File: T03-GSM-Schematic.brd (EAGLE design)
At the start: 33.9 x 80.5 mm, 19 parts, among them IC1 788TV, J1 POWER_JACKPTH_BREAD, J2 AVR, Q2 16M, U1 ATMEGA328P-PU

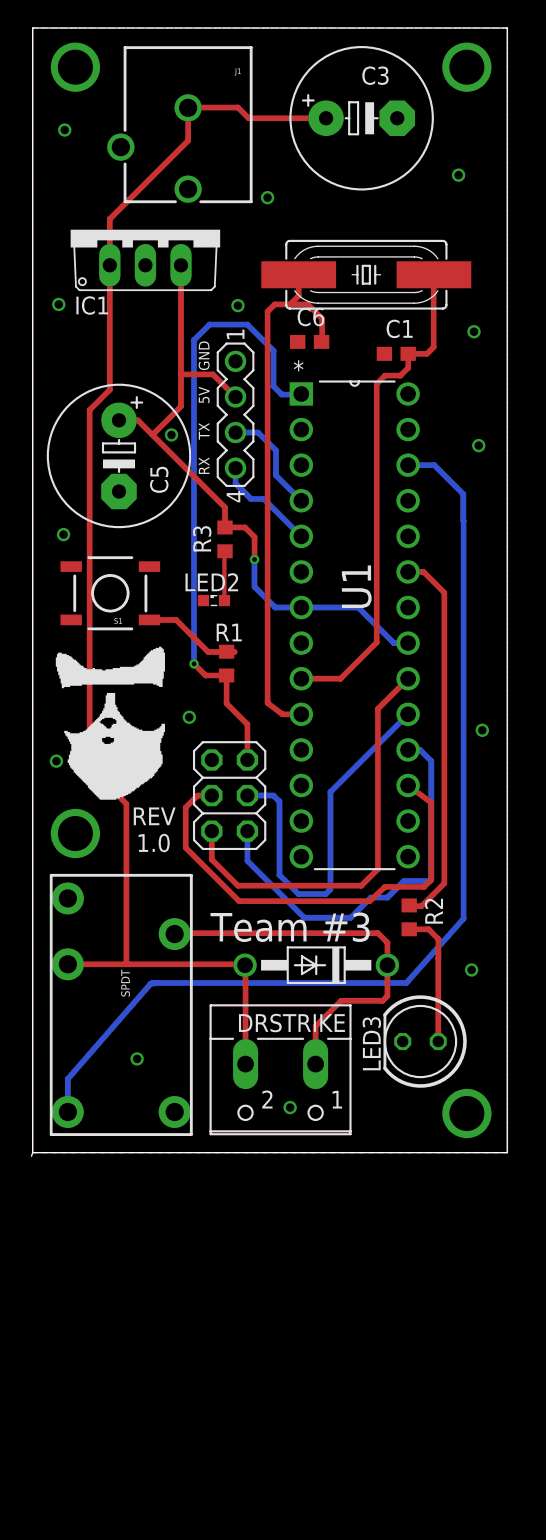
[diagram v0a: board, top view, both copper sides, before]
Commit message: Add files via upload
added flyback diode, bypass caps.  No board level work done yet.
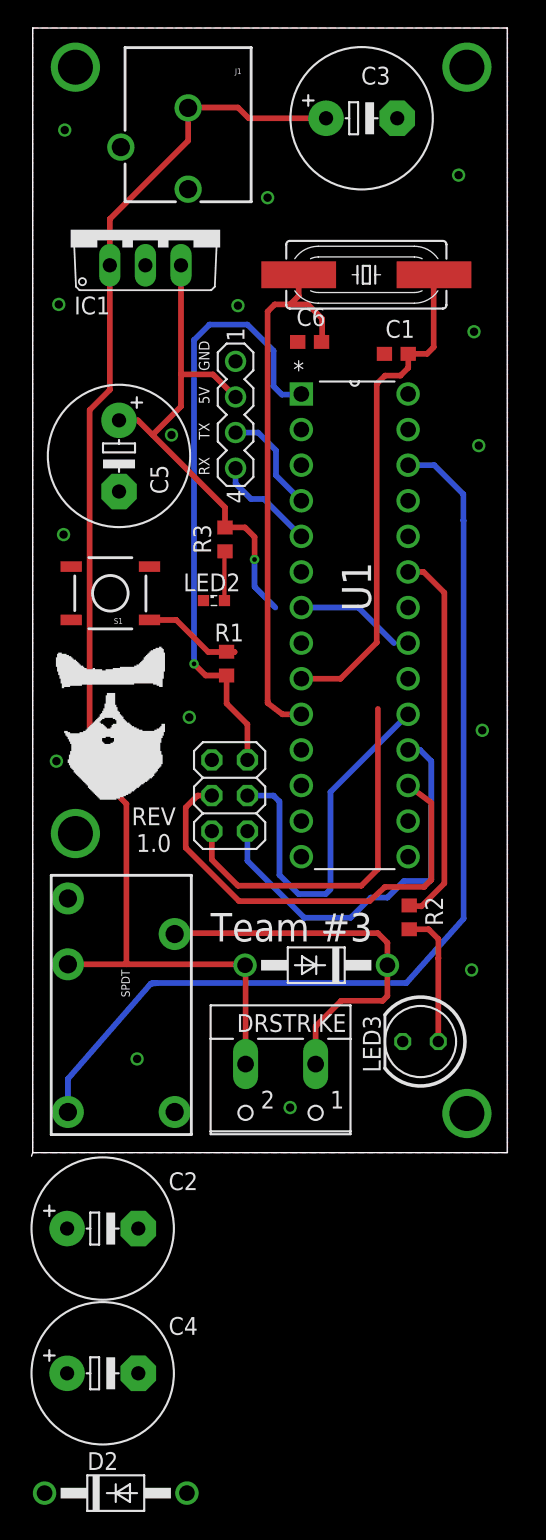
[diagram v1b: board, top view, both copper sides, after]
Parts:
- added C2, C4: 100n, rcl:E5-10,5
- added D2: 1N4004, diode:DO41-10
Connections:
- net 12V renamed +12V
- removed net 5V: C5.+, IC1.3, J2.2, R3.2, SV1.2, U1.20, U1.21, U1.7
- new net +5V: C2.+, C4.+, C5.+, IC1.3, J2.2, R3.2, SV1.2
- new net N$1: C2.-, U1.20, U1.21
- new net N$11: C4.-, U1.7
- net GND: now also D2.A
- net N$14: now also D2.C
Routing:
- net 5V: track 77.3 -> 0.00 mm, vias 1 -> 0
- net +5V: track 0.00 -> 63.7 mm, vias 0 -> 1
- net N$11: track 0.00 -> 7.66 mm

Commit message: Changed the layout of the PCB board
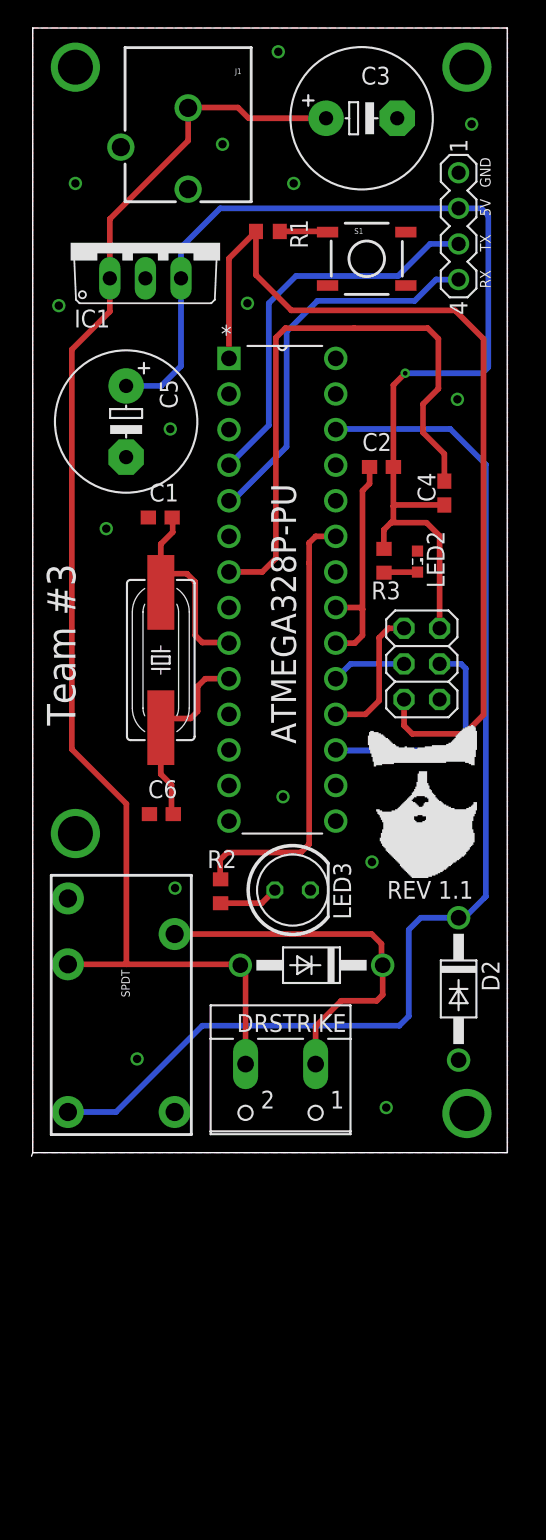
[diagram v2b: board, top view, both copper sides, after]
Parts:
- C2, C4: device rcl:E5-10,5 -> rcl:C0603
- moved C4 67.4 mm to (29.4, 47.1), turned to 90 degrees
- moved C2 57.9 mm to (24.9, 48.9), turned to 180 degrees
- moved D2 43.5 mm to (30.4, 11.7), turned to 270 degrees
- moved C6 35.3 mm to (9.18, 24.2)
- moved Q2 31.2 mm to (9.14, 35.2), turned to 90 degrees
- moved R1 31.0 mm to (16.8, 65.7), turned to 180 degrees
- moved S1 30.1 mm to (23.8, 63.8), turned to 0 degrees
- moved SV1 20.8 mm to (30.4, 66.1)
- moved C1 20.5 mm to (9.10, 45.3)
- moved J2 16.6 mm to (27.8, 34.9), turned to 270 degrees
- moved LED2 14.8 mm to (27.5, 42.2), turned to 270 degrees
- moved LED3 14.1 mm to (18.5, 18.7), turned to 0 degrees
- moved R2 13.6 mm to (13.4, 18.7)
- moved R3 11.4 mm to (25.1, 42.2)
- moved U1 5.75 mm to (21.6, 23.7)
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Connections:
- net +5V: now also C2.1, C4.1; no longer C2.+, C4.+
- net N$1: now also C2.2; no longer C2.-
- net N$11: now also C4.2; no longer C4.-
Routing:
- net N$11: track 7.66 -> 42.9 mm
- net N$18: track 39.6 -> 13.9 mm
- net N$10: track 44.1 -> 66.3 mm, vias 1 -> 0
- net N$5: track 26.8 -> 5.31 mm
- net N$16: track 35.8 -> 14.9 mm
- net RX: track 7.35 -> 27.7 mm
- net TX: track 7.75 -> 28.0 mm
- net N$8: track 28.5 -> 10.0 mm
- net +5V: track 63.7 -> 80.5 mm
- net N$1: track 0.00 -> 16.3 mm
- net N$7: track 32.4 -> 16.6 mm
- net N$14: track 71.3 -> 82.4 mm
- net N$6: track 9.69 -> 4.26 mm
- net N$9: track 27.1 -> 31.8 mm
- net N$2: track 7.59 -> 3.43 mm
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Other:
- board text added: "REV 1.1"
- board text removed: "REV 1.0"

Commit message: Add files via upload
Added test point, fixed ERC error.
More updates to come.
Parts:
- added R4: 0, rcl:0204/5
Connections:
- new net N$12: R4.2, U1.28
- net GND: now also R4.1
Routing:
- net N$6: track 4.26 -> 0.00 mm
- net N$12: track 0.00 -> 4.13 mm
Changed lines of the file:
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@@
 <?xml version="1.0" encoding="utf-8"?>
 <!DOCTYPE eagle SYSTEM "eagle.dtd">
-<eagle version="7.7.0">
+<eagle version="7.6.0">
 <drawing>
 <settings>
@@
 <element name="C4" library="rcl" package="C0603" value="100n" x="29.376390625" y="47.06995625" rot="R90"/>
 <element name="D2" library="diode" package="DO41-10" value="1N4004" x="30.392290625" y="11.68285" rot="R270"/>
+<element name="R4" library="rcl" package="0204/5" value="0" x="28.106521875" y="57.144284375" smashed="yes" rot="R180">
+<attribute name="NAME" x="28.673934375" y="57.584390625" size="0.9906" layer="25" ratio="10" rot="R180"/>
+<attribute name="VALUE" x="29.732175" y="57.59320625" size="0.9906" layer="27" ratio="10" rot="R180"/>
+</element>
 </elements>
 <signals>
@@
 <via x="10.158984375" y="18.878778125" extent="1-16" drill="0.6"/>
 <contactref element="D2" pad="A"/>
+<contactref element="R4" pad="1"/>
+<wire x1="30.392290625" y1="69.92805" x2="31.32353125" y2="73.398665625" width="0" layer="19" extent="1-1"/>
+<wire x1="26.013709375" y1="73.816803125" x2="31.32353125" y2="73.398665625" width="0" layer="19" extent="1-1"/>
+<wire x1="18.624803125" y1="69.16575" x2="26.013709375" y2="73.816803125" width="0" layer="19" extent="1-1"/>
+<wire x1="13.5453125" y1="71.959471875" x2="18.624803125" y2="69.16575" width="0" layer="19" extent="1-1"/>
+<wire x1="11.090225" y1="68.75708125" x2="13.5453125" y2="71.959471875" width="0" layer="19" extent="1-1"/>
+<wire x1="8.042528125" y1="62.3928375" x2="11.090225" y2="68.75708125" width="0" layer="19" extent="1-1"/>
+<wire x1="1.862484375" y1="60.445959375" x2="8.042528125" y2="62.3928375" width="0" layer="19" extent="1-1"/>
+<wire x1="15.3231375" y1="60.615278125" x2="8.042528125" y2="62.3928375" width="0" layer="19" extent="1-1"/>
+<wire x1="21.04239375" y1="61.88321875" x2="15.3231375" y2="60.615278125" width="0" layer="19" extent="1-1"/>
+<wire x1="17.52424375" y1="78.56281875" x2="13.5453125" y2="71.959471875" width="0" layer="19" extent="1-1"/>
+<wire x1="3.047696875" y1="69.165753125" x2="11.090225" y2="68.75708125" width="0" layer="19" extent="1-1"/>
+<wire x1="9.82035" y1="51.641496875" x2="15.3231375" y2="60.615278125" width="0" layer="19" extent="1-1"/>
+<wire x1="6.667271875" y1="49.634525" x2="9.82035" y2="51.641496875" width="0" layer="19" extent="1-1"/>
+<wire x1="8.250834375" y1="45.323878125" x2="6.667271875" y2="49.634525" width="0" layer="19" extent="1-1"/>
+<wire x1="5.2488125" y1="44.530215625" x2="8.250834375" y2="45.323878125" width="0" layer="19" extent="1-1"/>
+<wire x1="14.00585" y1="38.899746875" x2="8.250834375" y2="45.323878125" width="0" layer="19" extent="1-1"/>
+<wire x1="21.62585" y1="41.439746875" x2="14.00585" y2="38.899746875" width="0" layer="19" extent="1-1"/>
+<wire x1="27.460459375" y1="42.92720625" x2="21.62585" y2="41.439746875" width="0" layer="19" extent="1-1"/>
+<wire x1="29.03788125" y1="32.339171875" x2="27.460459375" y2="42.92720625" width="0" layer="19" extent="1-1"/>
+<wire x1="30.30763125" y1="53.75795625" x2="27.460459375" y2="42.92720625" width="0" layer="19" extent="1-1"/>
+<wire x1="24.2122375" y1="20.741265625" x2="29.03788125" y2="32.339171875" width="0" layer="19" extent="1-1"/>
+<wire x1="19.81871875" y1="18.738953125" x2="24.2122375" y2="20.741265625" width="0" layer="19" extent="1-1"/>
+<wire x1="17.862878125" y1="25.397453125" x2="19.81871875" y2="18.738953125" width="0" layer="19" extent="1-1"/>
+<wire x1="8.331021875" y1="24.159325" x2="17.862878125" y2="25.397453125" width="0" layer="19" extent="1-1"/>
+<wire x1="10.158984375" y1="18.878778125" x2="8.331021875" y2="24.159325" width="0" layer="19" extent="1-1"/>
+<wire x1="2.51" y1="18.14" x2="10.158984375" y2="18.878778125" width="0" layer="19" extent="1-1"/>
+<wire x1="7.44991875" y1="6.688" x2="10.158984375" y2="18.878778125" width="0" layer="19" extent="1-1"/>
+<wire x1="10.13" y1="2.9" x2="7.44991875" y2="6.688" width="0" layer="19" extent="1-1"/>
+<wire x1="30.646521875" y1="57.144284375" x2="10.13" y2="2.9" width="0" layer="19" extent="1-1"/>
+<wire x1="25.22814375" y1="3.217021875" x2="10.13" y2="2.9" width="0" layer="19" extent="1-1"/>
+<wire x1="30.392290625" y1="6.60285" x2="25.22814375" y2="3.217021875" width="0" layer="19" extent="1-1"/>
 </signal>
 <signal name="N$3">
@@
 <wire x1="24.889509375" y1="13.461165625" x2="24.974678125" y2="13.375996875" width="0.4064" layer="1"/>
 </signal>
-<signal name="N$6">
-<contactref element="R2" pad="2"/>
-<contactref element="LED3" pad="A"/>
-<wire x1="13.4077375" y1="17.8025625" x2="16.342328125" y2="17.8025625" width="0.4064" layer="1"/>
-<wire x1="16.342328125" y1="17.8025625" x2="17.27871875" y2="18.738953125" width="0.4064" layer="1"/>
-</signal>
 <signal name="N$9">
 <contactref element="R2" pad="1"/>
@@
 <wire x1="27.852546875" y1="53.419325" x2="28.953103125" y2="54.51988125" width="0.4064" layer="1"/>
 <wire x1="28.953103125" y1="54.51988125" x2="28.953103125" y2="58.075528125" width="0.4064" layer="1"/>
-<wire x1="28.953103125" y1="58.075528125" x2="28.19118125" y2="58.83745" width="0.4064" layer="1"/>
-<wire x1="28.19118125" y1="58.83745" x2="22.942375" y2="58.83745" width="0.4064" layer="1"/>
+<wire x1="28.953103125" y1="58.075528125" x2="28.44515625" y2="58.75279375" width="0.4064" layer="1"/>
+<wire x1="28.44515625" y1="58.75279375" x2="22.942375" y2="58.83745" width="0.4064" layer="1"/>
 <wire x1="22.942375" y1="58.83745" x2="22.942371875" y2="58.837446875" width="0.4064" layer="1"/>
 <wire x1="14.00585" y1="41.439746875" x2="16.38091875" y2="41.439746875" width="0.4064" layer="1"/>
@@
 <wire x1="30.39216875" y1="67.387928125" x2="30.392290625" y2="67.38805" width="0.4064" layer="16"/>
 </signal>
+<signal name="N$12">
+<contactref element="R4" pad="2"/>
+<contactref element="U1" pad="28"/>
+<wire x1="21.62585" y1="56.679746875" x2="23.239759375" y2="56.679746875" width="0.4064" layer="16"/>
+<wire x1="23.239759375" y1="56.679746875" x2="23.704296875" y2="57.144284375" width="0.4064" layer="16"/>
+<wire x1="23.704296875" y1="57.144284375" x2="25.566521875" y2="57.144284375" width="0.4064" layer="16"/>
+</signal>
+<signal name="N$6">
+<contactref element="R2" pad="2"/>
+<contactref element="LED3" pad="A"/>
+<wire x1="13.4077375" y1="17.8025625" x2="17.27871875" y2="18.738953125" width="0" layer="19" extent="1-1"/>
+</signal>
 </signals>

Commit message: Add files via upload
Added another test point after the voltage limiter and increased line thickness on power leads
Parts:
- added R5: 0, rcl:0204/5
- moved C6 1.34 mm to (9.96, 23.1), turned to 270 degrees
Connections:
- net +5V: now also R5.2
- net GND: now also R5.1
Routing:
- net +12V: track 96.6 -> 102.3 mm
- net +5V: track 80.5 -> 83.3 mm

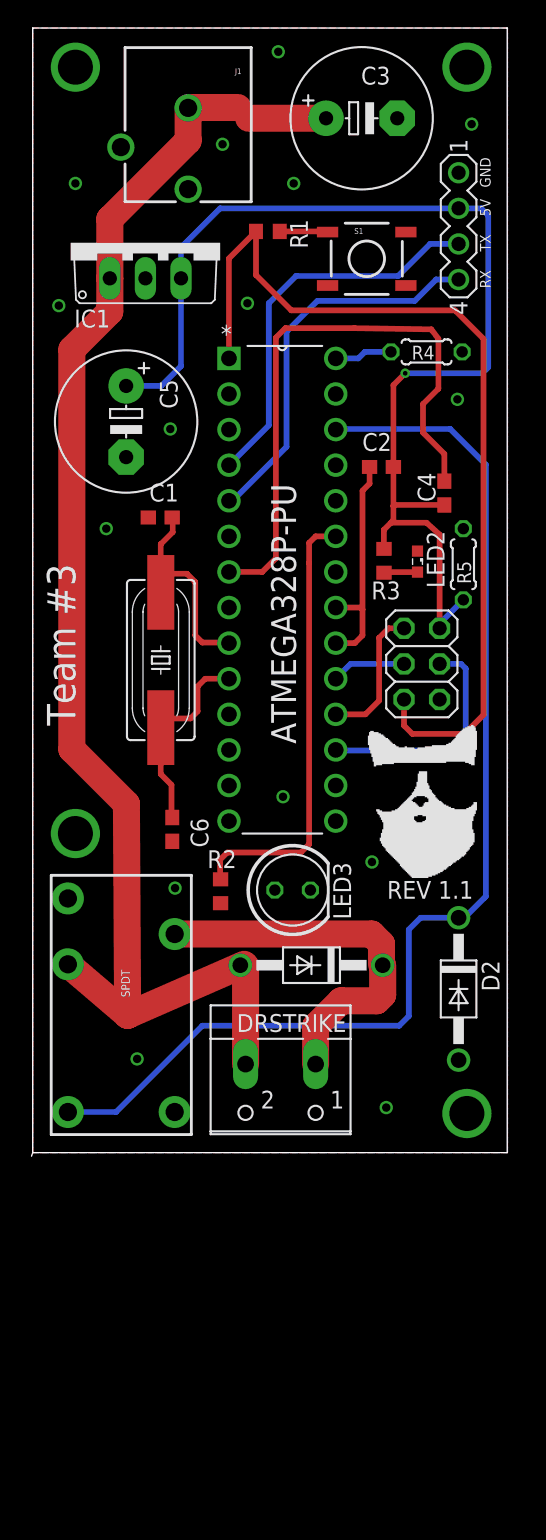
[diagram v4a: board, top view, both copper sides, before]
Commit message: Made the 5V line thicker
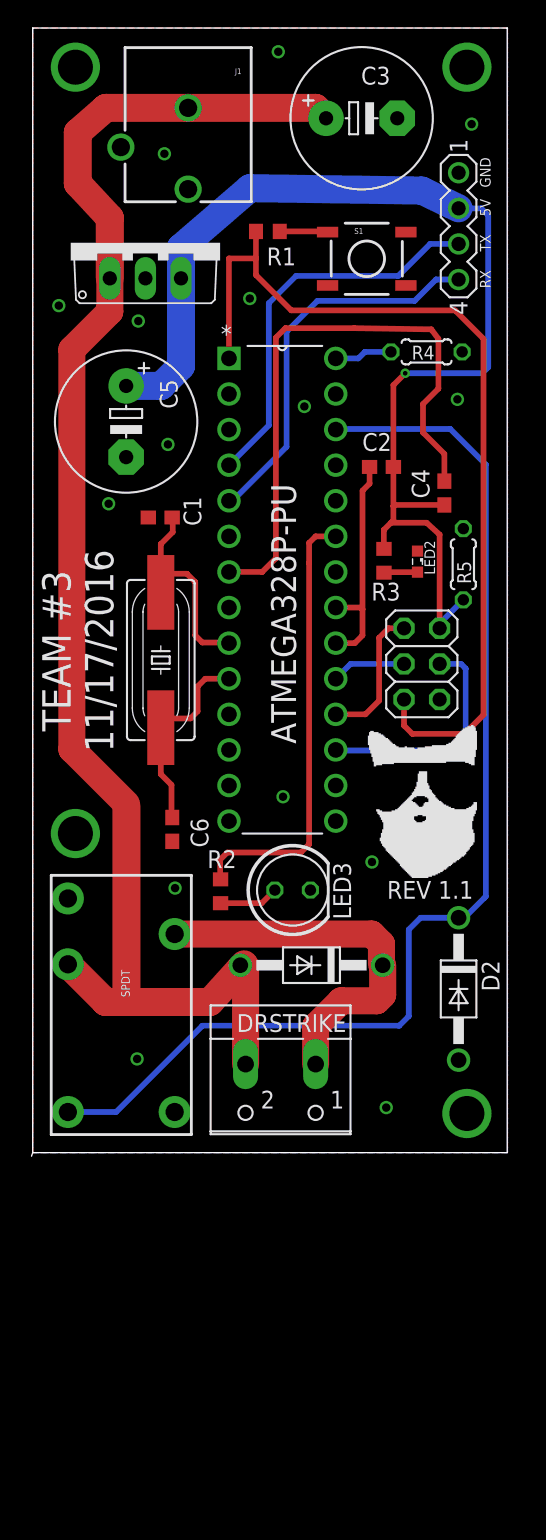
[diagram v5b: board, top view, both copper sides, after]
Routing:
- net +12V: track 102.3 -> 107.0 mm
- net N$6: track 0.00 -> 4.26 mm
- net N$10: track 66.3 -> 65.5 mm
- net +5V: track 83.3 -> 84.0 mm
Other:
- board text added: "TEAM #3 11/17/2016"
- board text removed: "Team #3"

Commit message: Add files via upload
Final Revision. 
No DRC or ERC errors.
Updates:
Power lines thickened
Power capacitor orientation fixed
Reset pull-up resistor added
Power symbols used in schematic
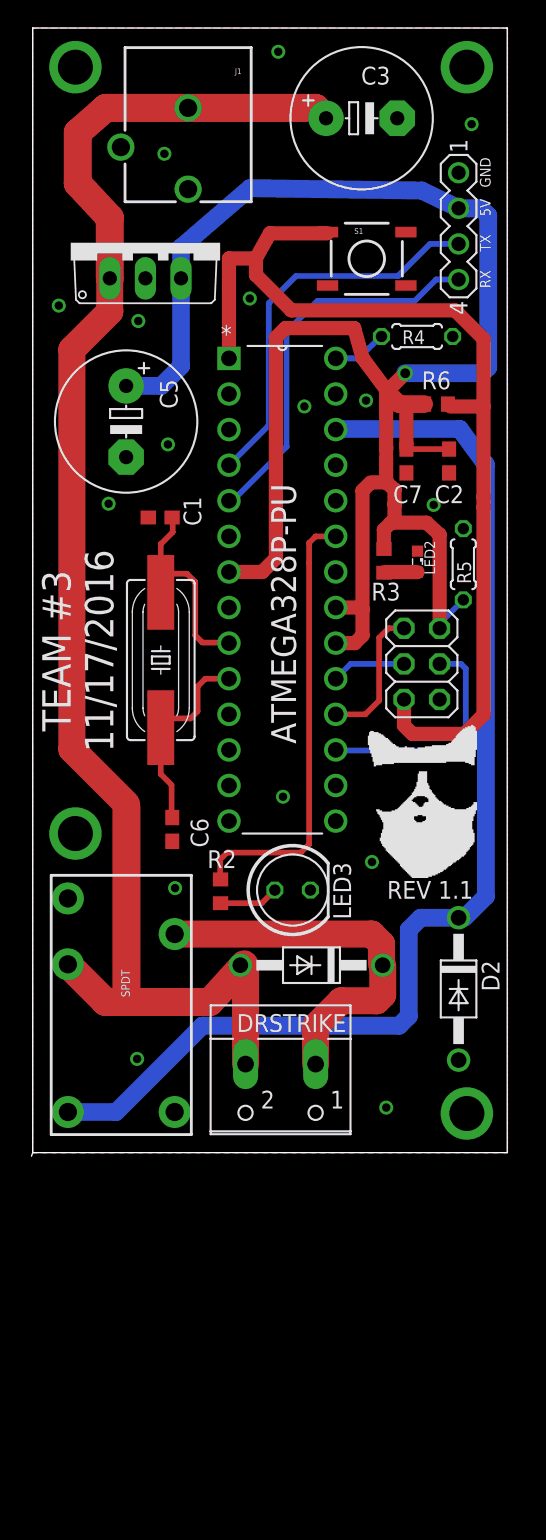
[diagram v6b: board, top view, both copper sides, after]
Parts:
- removed C4: 100n, rcl:C0603
- removed R1: 10k, rcl:R0603
- added C7: 100n, rcl:C0603
- added R6: 10k, rcl:R0603
- moved C2 4.84 mm to (29.7, 49.4), turned to 90 degrees
- moved R4 1.29 mm to (27.4, 58.2)
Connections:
- removed net N$1: C2.2, U1.20, U1.21
- removed net N$10: J2.5, R1.2, U1.1
- removed net N$11: C4.2, U1.7
- net +5V: now also C2.2, C7.2, R6.2, U1.20, U1.21, U1.7; no longer C2.1, C4.1
- net GND: now also C2.1, C7.1
- net N$2: now also J2.5, R6.1, U1.1; no longer R1.1
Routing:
- net N$2: track 3.43 -> 72.5 mm
- net N$10: track 65.5 -> 0.00 mm
- net +5V: track 84.0 -> 140.0 mm
- net N$11: track 43.0 -> 0.00 mm
- net N$1: track 16.3 -> 0.00 mm, vias 0 -> 1

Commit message: Made the board litter wider
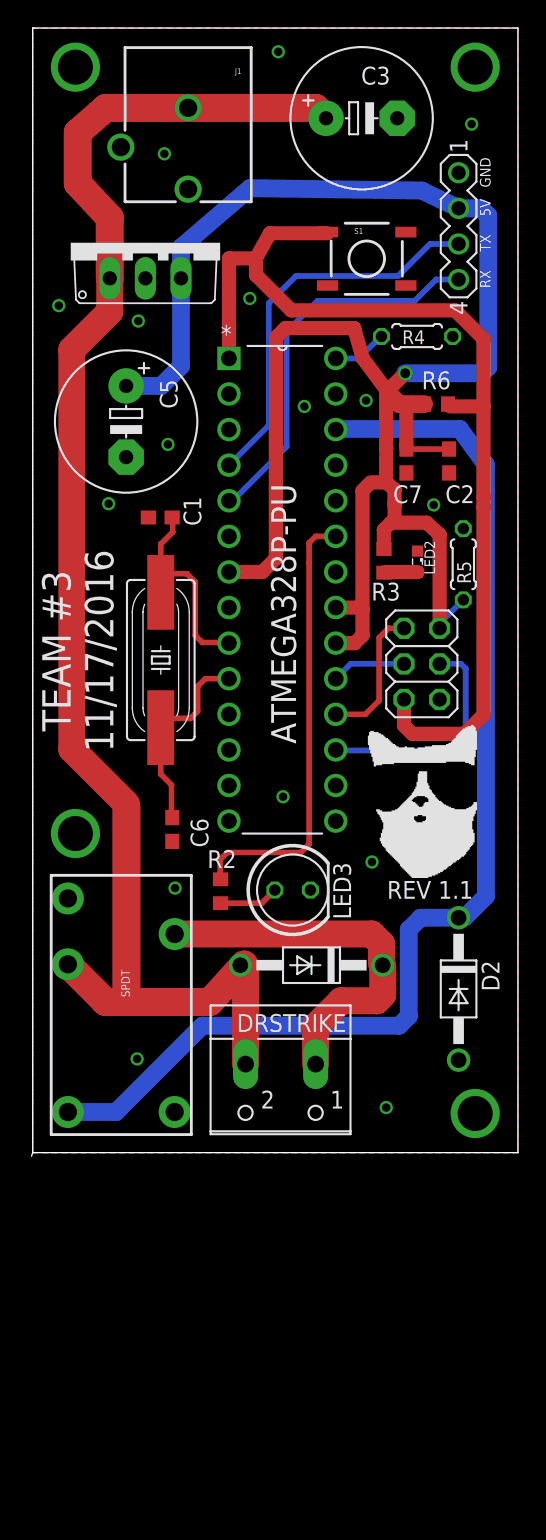
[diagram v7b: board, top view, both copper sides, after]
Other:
- board size 33.9 x 80.5 mm -> 34.7 x 80.5 mm
